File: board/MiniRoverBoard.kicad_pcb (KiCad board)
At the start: 2 copper layers, 49 parts, among them J1 DEBUG, Q1 NMOS, Q2 BSS138, U2 OKI, U3 Opamp_Dual, U4 LT1910, U7 ESP32-S2-DEVKITM-1U, U8 Opamp_Dual

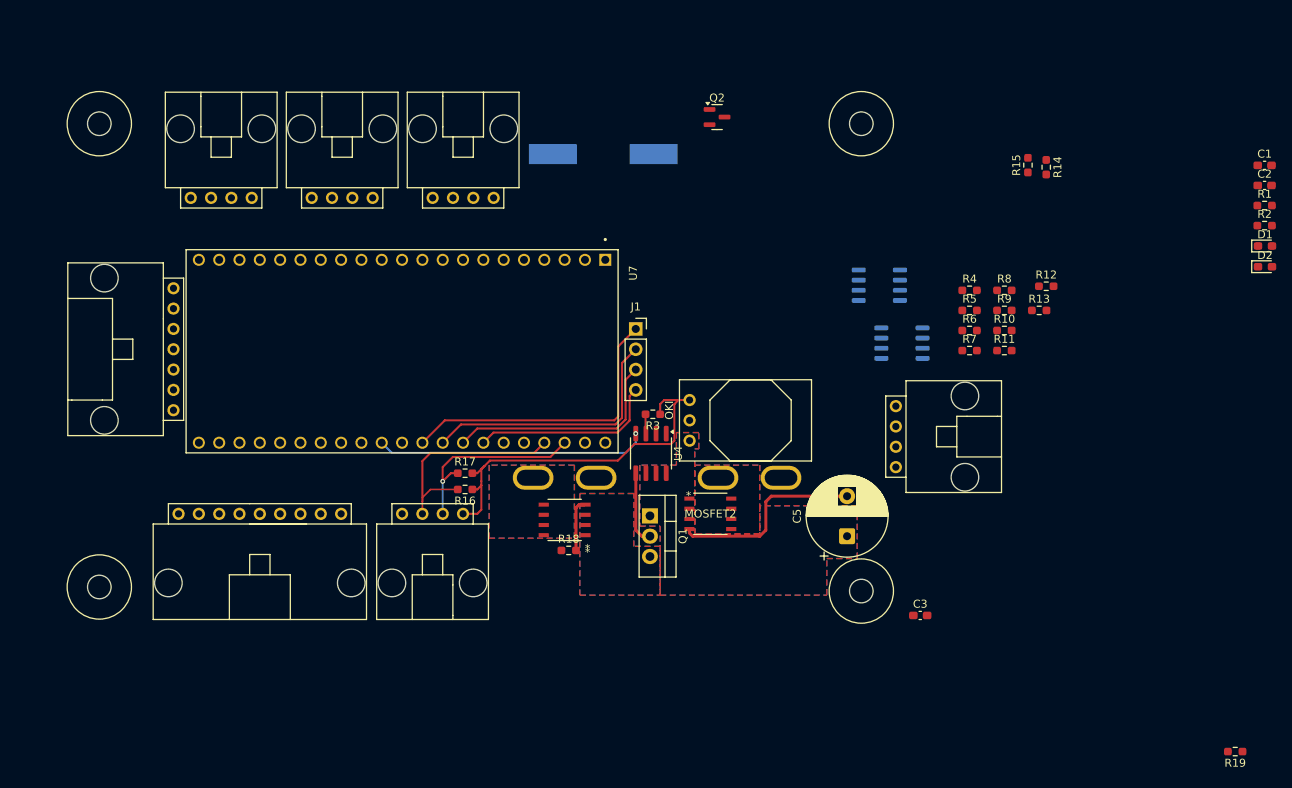
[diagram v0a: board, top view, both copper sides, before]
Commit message: general layout placed + ground plate
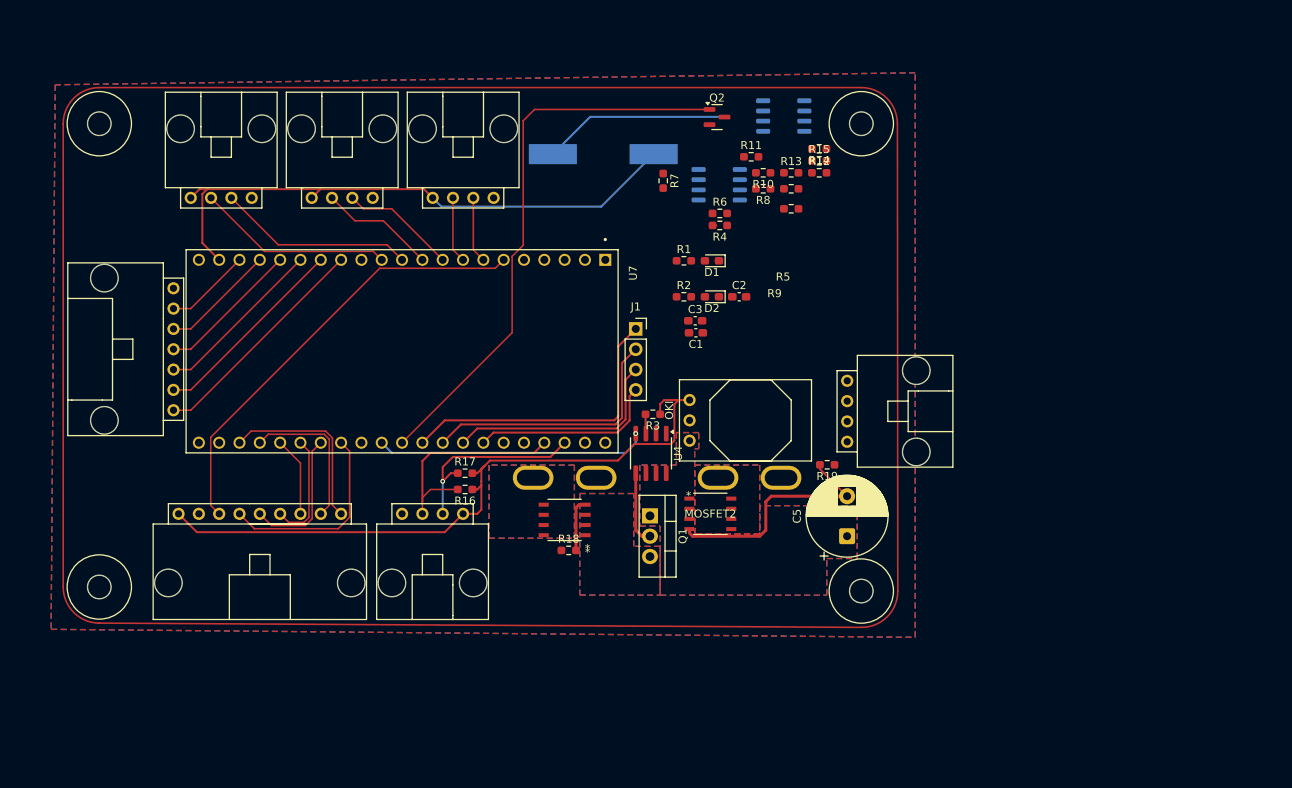
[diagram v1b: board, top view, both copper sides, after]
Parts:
- moved C1 74.1 mm to (123.1, 65.0), turned to 180 degrees
- moved R2 73.1 mm to (121.6, 60.5)
- moved R1 72.9 mm to (121.6, 56.0)
- moved D2 69.2 mm to (125.1, 60.5), turned to 180 degrees
- moved D1 69.2 mm to (125.1, 56.0), turned to 180 degrees
- moved C2 67.1 mm to (128.5, 60.5)
- moved R19 62.3 mm to (139.5, 81.5)
- moved C3 46.3 mm to (123.0, 63.5)
- moved R7 43.8 mm to (119.0, 46.0), turned to -90 degrees
- moved R11 39.9 mm to (130.0, 43.0)
- moved R10 36.0 mm to (131.5, 45.0), turned to 180 degrees
- moved R13 35.4 mm to (135.0, 45.0)
- moved R6 34.5 mm to (126.1, 50.1)
- moved R8 32.7 mm to (131.5, 47.0), turned to 180 degrees
- moved R4 32.3 mm to (126.1, 51.6), turned to 180 degrees
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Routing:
- net +5V: track 46.8 -> 158.3 mm
- net Buzzer_Pin: track 0.00 -> 70.4 mm
- net ESC_CURRENT: track 0.00 -> 55.8 mm
- net SPI_MISO: track 0.00 -> 28.7 mm
- net TFT_Reset: track 0.00 -> 25.1 mm
- net ESC_PWM_1: track 0.00 -> 24.9 mm
- net ENCODER_PWN_J3: track 0.00 -> 24.6 mm
- net SERVO_PWN_J3: track 0.00 -> 24.5 mm
- net Net-(B1-V-): track 0.00 -> 23.7 mm
- net ESC_PWM_6: track 0.00 -> 22.5 mm
- net SPI_CLK: track 0.00 -> 21.6 mm
- net ESC_PWM_5: track 0.00 -> 19.1 mm
- net SPI_MOSI: track 0.00 -> 18.0 mm
- net ESC_PWM_2: track 0.00 -> 17.4 mm
- net SERVO_PWN_J2: track 0.00 -> 14.5 mm
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- added copper zone on B.Cu, net GND
- added copper zone on F.Cu, net GND

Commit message: Add Organized OpAmp Components
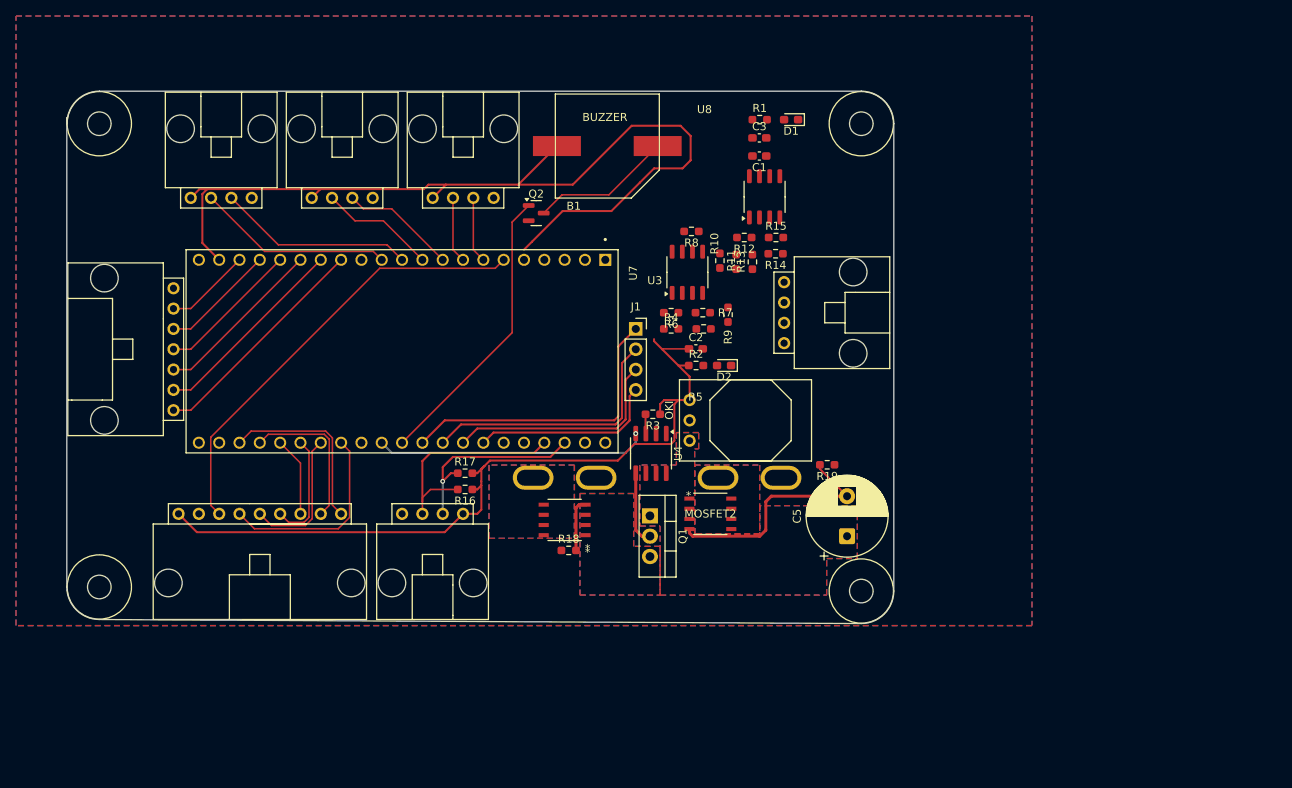
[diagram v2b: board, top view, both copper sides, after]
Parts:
- B1, U3, U8: moved to F.Cu
- moved Q2 25.6 mm to (103.1, 50.0)
- moved C3 24.2 mm to (131.0, 40.6)
- moved C1 23.5 mm to (131.0, 42.9)
- moved D1 20.2 mm to (135.0, 38.4)
- moved R1 20.0 mm to (131.1, 38.4)
- moved R5 18.6 mm to (124.1, 64.5)
- moved R9 17.6 mm to (127.1, 62.7), turned to 90 degrees
- moved R7 17.2 mm to (124.0, 62.5), turned to 0 degrees
- moved Conn4 14.6 mm to (134.1, 58.7)
- moved R4 14.3 mm to (120.0, 64.5), turned to 0 degrees
- moved R14 14.2 mm to (133.0, 55.1)
- moved R6 13.8 mm to (120.0, 62.5), turned to 180 degrees
- moved R11 13.6 mm to (126.1, 56.0), turned to -90 degrees
- moved B1 12.5 mm to (105.5, 41.7), turned to 0 degrees
- moved R12 12.4 mm to (129.1, 53.1), turned to 180 degrees
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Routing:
- net +5V: track 158.3 -> 214.9 mm
- net Buzzer_Pin: track 70.4 -> 36.2 mm
- net Net-(B1-V-): track 23.7 -> 17.7 mm
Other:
- board outline added: 103.4 x 66.5 mm

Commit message: Add 5V trace
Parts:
- moved C3 13.5 mm to (142.5, 47.8), turned to 90 degrees
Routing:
- net +5V: track 214.9 -> 192.5 mm, vias 0 -> 2
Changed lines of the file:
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@@
 	(footprint "Capacitor_SMD:C_0603_1608Metric_Pad1.08x0.95mm_HandSolder"
 		(layer "F.Cu")
-		(at 131.0205 40.64)
+		(at 142.494 47.752 90)
 		(descr "Capacitor SMD 0603 (1608 Metric), square (rectangular) end terminal, IPC-7351 nominal with elongated pad for handsoldering. (Body size source: IPC-SM-782 page 76, https://www.pcb-3d.com/wordpress/wp-content/uploads/ipc-sm-782a_amendment_1_and_2.pdf), generated with kicad-footprint-generator")
 		(tags "capacitor handsolder")
 		(property "Reference" "C3"
-			(at 0 -1.43 0)
+			(at 0 -1.43 90)
 			(layer "F.SilkS")
 			(effects
@@
 		)
 		(property "Value" "10uF"
-			(at 23 -11.57 0)
+			(at 23 -11.57 90)
 			(layer "F.Fab")
 			(effects
@@
 		)
 		(property "Datasheet" ""
-			(at 0 0 0)
+			(at 0 0 90)
 			(layer "F.Fab")
 			(hide yes)
@@
 		)
 		(property "Description" "capacitor, US symbol"
-			(at 0 0 0)
+			(at 0 0 90)
 			(layer "F.Fab")
 			(hide yes)
@@
 		)
 		(fp_line
-			(start -1.65 -0.73)
-			(end 1.65 -0.73)
+			(start 1.65 -0.73)
+			(end 1.65 0.73)
 			(stroke
 				(width 0.05)
@@
 		)
 		(fp_line
-			(start -1.65 0.73)
-			(end -1.65 -0.73)
+			(start -1.65 -0.73)
+			(end 1.65 -0.73)
 			(stroke
 				(width 0.05)
@@
 		)
 		(fp_line
-			(start 1.65 -0.73)
-			(end 1.65 0.73)
+			(start 1.65 0.73)
+			(end -1.65 0.73)
 			(stroke
 				(width 0.05)
@@
 		)
 		(fp_line
-			(start 1.65 0.73)
-			(end -1.65 0.73)
+			(start -1.65 0.73)
+			(end -1.65 -0.73)
 			(stroke
 				(width 0.05)
@@
 		)
 		(fp_line
-			(start -0.8 -0.4)
-			(end 0.8 -0.4)
+			(start 0.8 -0.4)
+			(end 0.8 0.4)
 			(stroke
 				(width 0.1)
@@
 		)
 		(fp_line
-			(start -0.8 0.4)
-			(end -0.8 -0.4)
+			(start -0.8 -0.4)
+			(end 0.8 -0.4)
 			(stroke
 				(width 0.1)
@@
 		)
 		(fp_line
-			(start 0.8 -0.4)
-			(end 0.8 0.4)
+			(start 0.8 0.4)
+			(end -0.8 0.4)
 			(stroke
 				(width 0.1)
@@
 		)
 		(fp_line
-			(start 0.8 0.4)
-			(end -0.8 0.4)
+			(start -0.8 0.4)
+			(end -0.8 -0.4)
 			(stroke
 				(width 0.1)
@@
 		)
 		(fp_text user "${REFERENCE}"
-			(at 0 0 0)
+			(at 0 0 90)
 			(layer "F.Fab")
 			(effects
@@
 		)
 		(pad "1" smd roundrect
-			(at -0.8625 0)
+			(at -0.8625 0 90)
 			(size 1.075 0.95)
 			(layers "F.Cu" "F.Mask" "F.Paste")
@@
 		)
 		(pad "2" smd roundrect
-			(at 0.8625 0)
+			(at 0.8625 0 90)
 			(size 1.075 0.95)
 			(layers "F.Cu" "F.Mask" "F.Paste")
@@
 	)
 	(segment
-		(start 106.426 49.784)
-		(end 102.616 53.594)
-		(width 0.254)
-		(layer "F.Cu")
-		(net 3)
-	)
-	(segment
 		(start 118.618 73.914)
 		(end 118.618 75.184)
@@
 	)
 	(segment
-		(start 122.428 43.434)
-		(end 121.412 44.45)
-		(width 0.254)
-		(layer "F.Cu")
-		(net 3)
-	)
-	(segment
 		(start 96.266 84.074)
 		(end 96.266 83.566)
@@
 	)
 	(segment
-		(start 115.062 39.116)
-		(end 121.158 39.116)
-		(width 0.254)
-		(layer "F.Cu")
-		(net 3)
-	)
-	(segment
 		(start 63.5 55.88)
 		(end 61.394 53.774)
@@
 	)
 	(segment
-		(start 112.522 49.784)
-		(end 106.426 49.784)
-		(width 0.254)
-		(layer "F.Cu")
-		(net 3)
-	)
-	(segment
 		(start 97.335 80.973)
 		(end 113.337 80.973)
@@
 	)
 	(segment
-		(start 100.888 46.482)
-		(end 107.696 46.482)
-		(width 0.254)
-		(layer "F.Cu")
-		(net 3)
-	)
-	(segment
-		(start 117.856 44.45)
-		(end 116.078 46.228)
-		(width 0.254)
-		(layer "F.Cu")
-		(net 3)
-	)
-	(segment
 		(start 95.758 84.582)
 		(end 96.266 84.074)
@@
 	)
 	(segment
-		(start 102.616 53.594)
-		(end 101.6 54.61)
-		(width 0.254)
-		(layer "F.Cu")
-		(net 3)
-	)
-	(segment
 		(start 58.42 87.63)
 		(end 60.713 89.923)
@@
 	)
 	(segment
-		(start 121.412 44.45)
-		(end 117.856 44.45)
+		(start 100.888 46.482)
+		(end 109.22 46.482)
 		(width 0.254)
 		(layer "F.Cu")
@@
 	)
 	(segment
-		(start 107.696 46.482)
-		(end 115.062 39.116)
-		(width 0.254)
-		(layer "F.Cu")
-		(net 3)
-	)
-	(segment
 		(start 120.904 73.406)
 		(end 119.126 73.406)
@@
 	)
 	(segment
-		(start 122.428 40.386)
-		(end 122.428 43.434)
-		(width 0.254)
-		(layer "F.Cu")
-		(net 3)
-	)
-	(segment
 		(start 95.758 87.63)
 		(end 96.266 87.122)
@@
 	)
 	(segment
-		(start 116.078 46.228)
-		(end 112.522 49.784)
-		(width 0.254)
-		(layer "F.Cu")
-		(net 3)
-	)
-	(segment
-		(start 121.158 39.116)
-		(end 122.428 40.386)
-		(width 0.254)
-		(layer "F.Cu")
-		(net 3)
-	)
-	(segment
 		(start 120.904 69.088)
 		(end 122.1925 69.088)
@@
 		(net 3)
 	)
+	(via
+		(at 117.856 65.786)
+		(size 0.6)
+		(drill 0.3)
+		(layers "F.Cu" "B.Cu")
+		(net 3)
+	)
+	(via
+		(at 109.22 46.482)
+		(size 0.6)
+		(drill 0.3)
+		(layers "F.Cu" "B.Cu")
+		(net 3)
+	)
+	(segment
+		(start 117.856 55.118)
+		(end 117.856 65.786)
+		(width 0.254)
+		(layer "B.Cu")
+		(net 3)
+	)
+	(segment
+		(start 109.22 46.482)
+		(end 117.856 55.118)
+		(width 0.254)
+		(layer "B.Cu")
+		(net 3)
+	)
